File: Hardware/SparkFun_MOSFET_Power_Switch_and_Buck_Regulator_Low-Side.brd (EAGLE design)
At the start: 38.1 x 38.1 mm, 84 parts, among them J1 PTH, J3 5.5x2.1mm Barrel, J4 1X04_SMD_STRAIGHT_COMBO, Q1 600mA/40V, Q2 100A/100V/6.8mΩ, U1 LMR14203

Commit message: text overlap in sch
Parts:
- J4: value 1X04_SMD_STRAIGHT_COMBO -> SMD
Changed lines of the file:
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@@
 <element name="U$25" library="output" package="POWER_1" value="" x="18.696940625" y="16.5735" smashed="yes" rot="MR0"/>
 <element name="U$26" library="output" package="SWITCH_2" value="" x="18.760440625" y="14.23161875" smashed="yes" rot="MR0"/>
-<element name="J4" library="SparkFun-Connectors" package="1X04_SMD_VERTICAL_COMBO" value="1X04_SMD_STRAIGHT_COMBO" x="33.02" y="22.86" smashed="yes" rot="R270">
+<element name="J4" library="SparkFun-Connectors" package="1X04_SMD_VERTICAL_COMBO" value="SMD" x="33.02" y="22.86" smashed="yes" rot="R270">
 <attribute name="NAME" x="35.878" y="23.241" size="0.6096" layer="25" font="vector" ratio="20" rot="R270"/>
 <attribute name="PROD_ID" value="CONN-08511" x="33.02" y="22.86" size="1.778" layer="27" rot="R270" display="off"/>

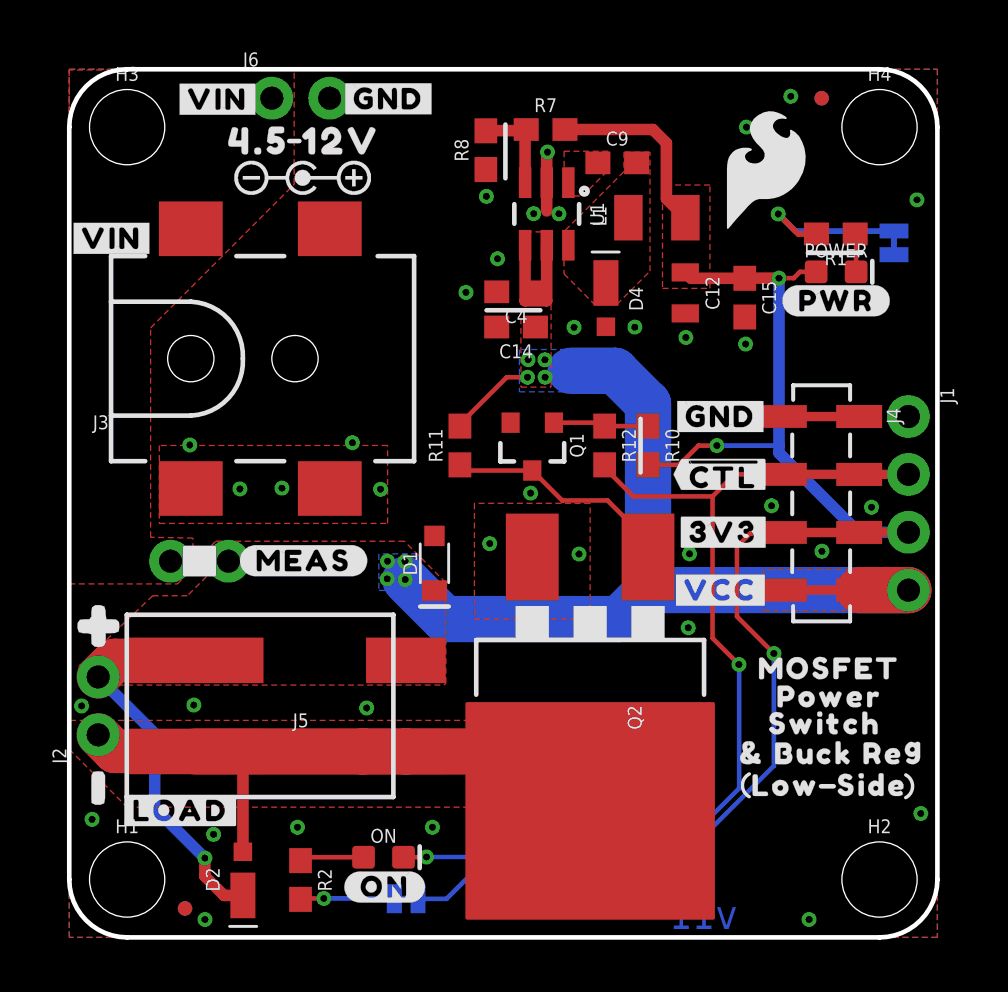
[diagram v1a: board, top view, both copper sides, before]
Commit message: group review final changes
-moved 4-pin header north 0.05inch to get all headers on same grid for perf board plug in ability.
-MEAS moved to on grid.
-upped material quality to TG155
-LED labels to text only style silk
-added exposed copper for heat sink under the MOSFET
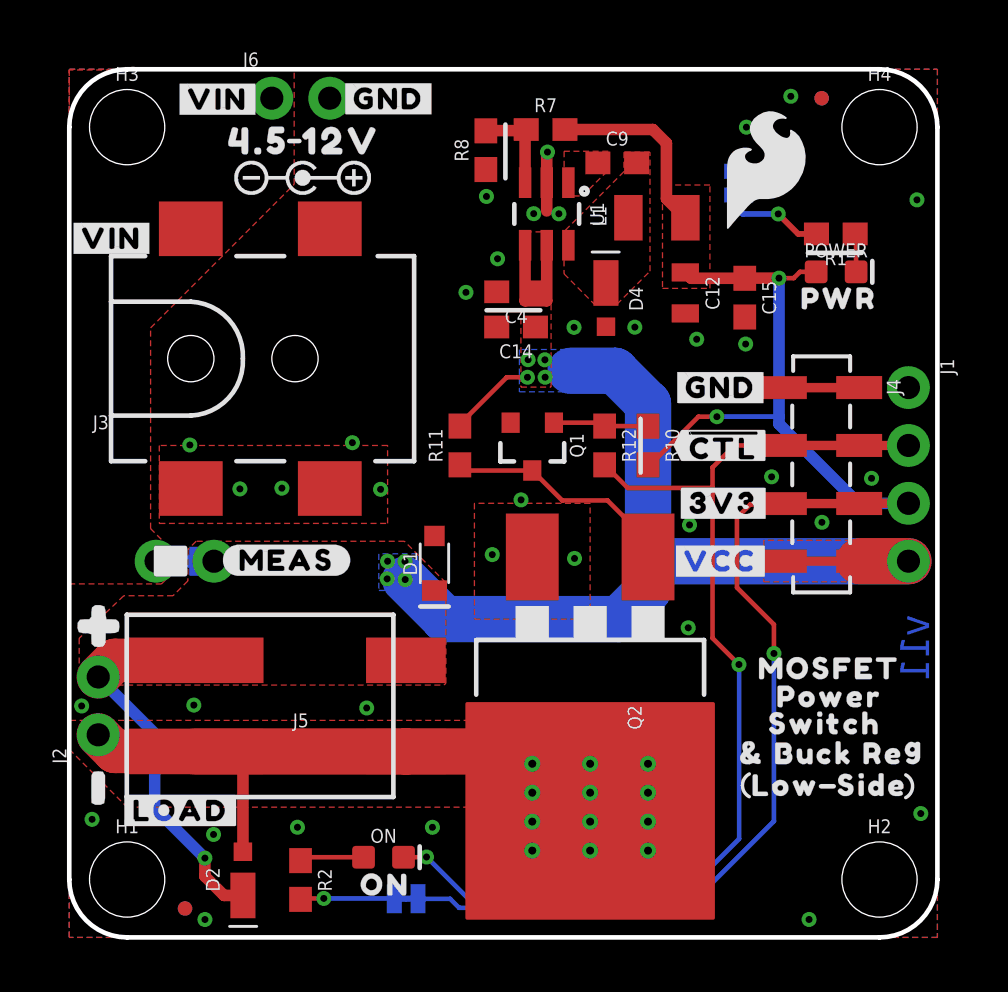
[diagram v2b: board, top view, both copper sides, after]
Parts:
- removed U$5: (no value), output:#PWR#9
- removed U$7: (no value), output:#ON#10
- added U$34: (no value), output:PWR9
- added U$35: (no value), output:ON10
- moved U$15 7.34 mm to (24.4, 33.1)
- moved PWR_LED 7.30 mm to (29.4, 33.1), turned to 270 degrees
- moved LOGO2 6.47 mm to (19.0, 28.4)
- moved U$43 4.24 mm to (21.0, 13.6)
- moved U$44 4.24 mm to (17.2, 13.6)
- moved U$39 4.04 mm to (22.6, 15.0)
- moved U$40 3.99 mm to (17.0, 15.0)
- moved U$42 3.88 mm to (18.8, 16.3)
- moved U$25 3.65 mm to (18.4, 20.2)
- moved U$26 3.65 mm to (18.5, 17.9)
- moved U$24 3.65 mm to (18.2, 22.3)
- moved U$31 1.27 mm to (28.6, 16.5)
- moved U$32 1.27 mm to (34.2, 16.5)
- moved J1 1.27 mm to (36.8, 24.1)
- moved J4 1.27 mm to (33.0, 24.1)
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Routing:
- net !CTL: track 43.7 -> 47.5 mm
- net N$6: track 7.43 -> 4.50 mm
- net 3.3V: track 73.5 -> 75.7 mm
- net LOAD: track 28.4 -> 29.1 mm, vias 0 -> 12
- added copper zone on layer 16, net LOAD
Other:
- board text added: "2-Layer Design Soldermask: Red Silkscreen: White Thickness: 1.6mm Copper Plating: 2 OZ Surface Finish: Lead-Free HASL Material: TG155"
- board text removed: "2-Layer Design Soldermask: Red Silkscreen: White Thickness: 1.6mm Copper Plating: 2 OZ Surface Finish: Lead-Free HASL Material: TG135-140"

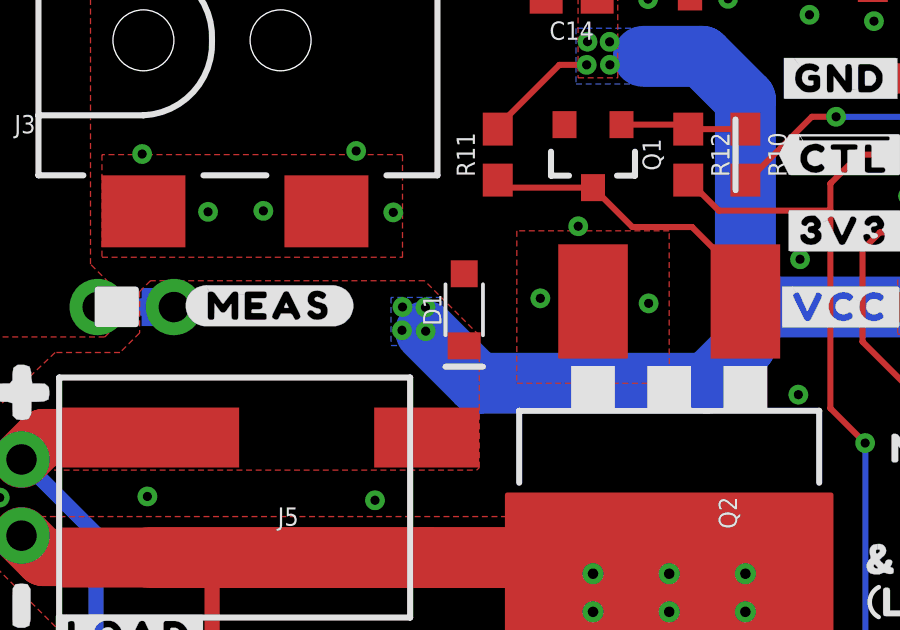
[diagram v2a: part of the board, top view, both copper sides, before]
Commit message: Removed D1 Zener
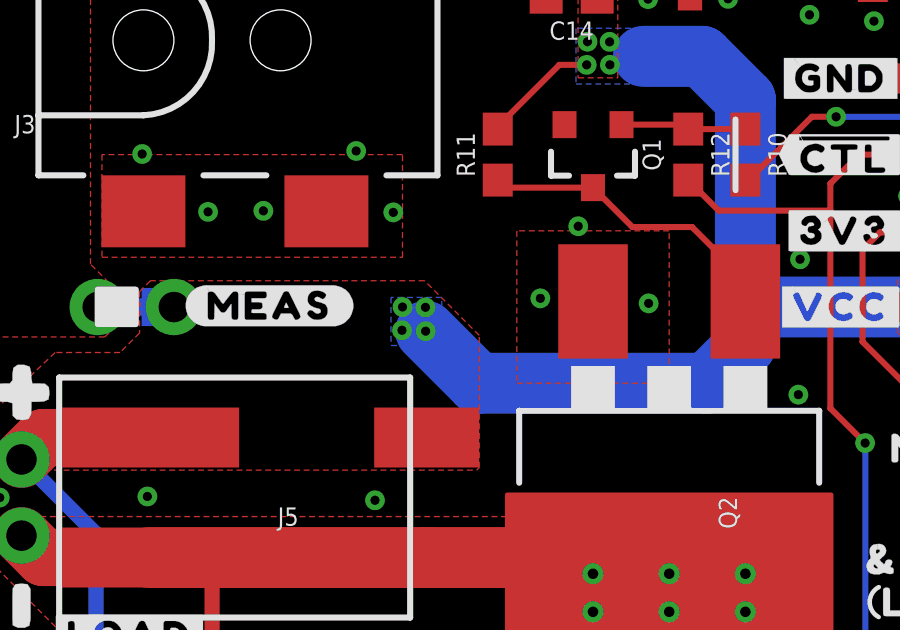
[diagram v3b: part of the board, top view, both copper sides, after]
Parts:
- removed D1: 15V, SparkFun-DiscreteSemi:PANASONIC_SMINI2-F5-B
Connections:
- net GND: no longer D1.A
- net VCC: no longer D1.C
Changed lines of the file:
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@@
 <drawing>
 <settings>
-<setting alwaysvectorfont="yes"/>
+<setting alwaysvectorfont="no"/>
 <setting keepoldvectorfont="yes"/>
 <setting verticaltext="up"/>
@@
 <element name="U$43" library="output" package="LOW0" value="" x="21.043903125" y="13.6194875" smashed="yes" rot="MR0"/>
 <element name="U$44" library="output" package="SIDE0" value="" x="17.233903125" y="13.6194875" smashed="yes" rot="MR0"/>
-<element name="D1" library="SparkFun-DiscreteSemi" package="PANASONIC_SMINI2-F5-B" value="15V" x="16.0274" y="16.418559375" smashed="yes" rot="R90">
-<attribute name="NAME" x="15.2654" y="16.418559375" size="0.6096" layer="25" font="vector" ratio="20" rot="R90" align="bottom-center"/>
-<attribute name="PROD_ID" value="DIO-12989" x="16.0274" y="16.418559375" size="1.778" layer="27" rot="R90" display="off"/>
-<attribute name="VALUE" x="16.7894" y="16.418559375" size="0.6096" layer="27" font="vector" ratio="20" rot="R90" align="top-center"/>
-</element>
 <element name="U$34" library="output" package="PWR9" value="" x="33.7693" y="28.039059375" smashed="yes"/>
 <element name="U$35" library="output" package="ON10" value="" x="13.85061875" y="2.308859375" smashed="yes"/>
@@
 </polygon>
 <via x="0.543559375" y="10.15745625" extent="1-16" drill="0.3048"/>
-<contactref element="D1" pad="A"/>
 </signal>
 <signal name="SDA1">
@@
 <wire x1="16.47698125" y1="13.97" x2="24.13" y2="13.97" width="2.032" layer="16"/>
 <wire x1="24.13" y1="13.97" x2="25.4" y2="15.24" width="2.032" layer="16"/>
-<contactref element="D1" pad="C"/>
 </signal>
 <signal name="N$1">
